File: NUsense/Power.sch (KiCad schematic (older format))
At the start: 36 parts, among them Q1201 BC807, Q1202 2N3055, Q1203 Q_NMOS_GDS, Q1204 Q_NMOS_GDS, Q1205 2N2219, Q1206 Q_PMOS_GDS, SW1201 SW_SPDT, U1201 LD1086D2M33

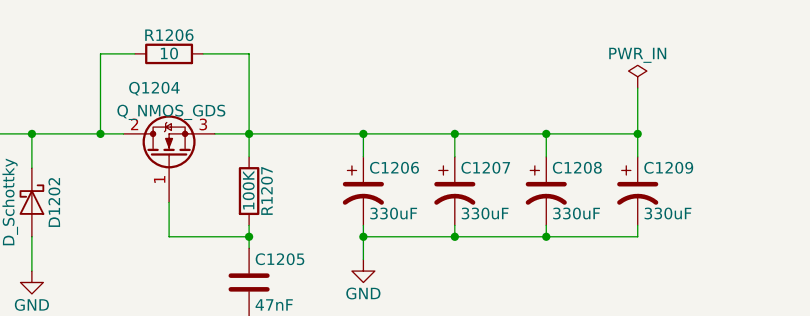
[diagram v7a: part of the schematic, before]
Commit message: Add LED and Button
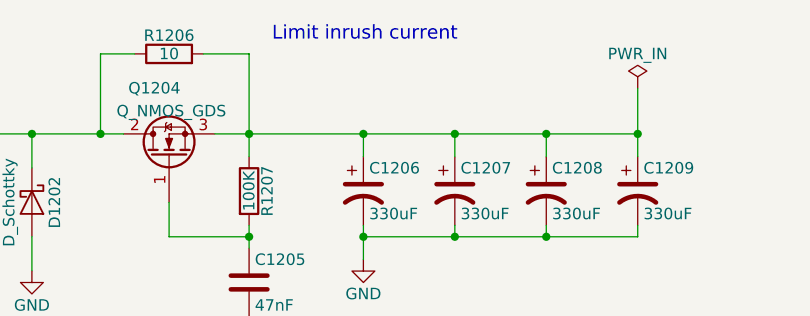
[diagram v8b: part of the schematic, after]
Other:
- note added: "Limit inrush current"
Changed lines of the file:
@@
 $EndDescr
 $Comp
-L GND #PWR0113
+L GND #PWR114
 U 1 1 5A69B4F4
 P 2700 1650
-F 0 "#PWR0113" H 2700 1400 50  0001 C CNN
+F 0 "#PWR114" H 2700 1400 50  0001 C CNN
 F 1 "GND" H 2700 1500 50  0000 C CNN
 F 2 "" H 2700 1650 50  0001 C CNN
@@
 $EndComp
 $Comp
-L GND #PWR0114
+L GND #PWR118
 U 1 1 5A69B8B6
 P 4500 3100
-F 0 "#PWR0114" H 4500 2850 50  0001 C CNN
+F 0 "#PWR118" H 4500 2850 50  0001 C CNN
 F 1 "GND" H 4500 2950 50  0000 C CNN
 F 2 "" H 4500 3100 50  0001 C CNN
@@
 $EndComp
 $Comp
-L GND #PWR0115
+L GND #PWR119
 U 1 1 5A69B8DD
 P 5400 3100
-F 0 "#PWR0115" H 5400 2850 50  0001 C CNN
+F 0 "#PWR119" H 5400 2850 50  0001 C CNN
 F 1 "GND" H 5400 2950 50  0000 C CNN
 F 2 "" H 5400 3100 50  0001 C CNN
@@
 Connection ~ 4150 1400
 $Comp
-L GND #PWR0116
+L GND #PWR120
 U 1 1 5A69BC53
 P 6150 2000
-F 0 "#PWR0116" H 6150 1750 50  0001 C CNN
+F 0 "#PWR120" H 6150 1750 50  0001 C CNN
 F 1 "GND" H 6150 1850 50  0000 C CNN
 F 2 "" H 6150 2000 50  0001 C CNN
@@
 $EndComp
 $Comp
-L GND #PWR0117
+L GND #PWR121
 U 1 1 5A69BC80
 P 6500 2000
-F 0 "#PWR0117" H 6500 1750 50  0001 C CNN
+F 0 "#PWR121" H 6500 1750 50  0001 C CNN
 F 1 "GND" H 6500 1850 50  0000 C CNN
 F 2 "" H 6500 2000 50  0001 C CNN
@@
 $EndComp
 $Comp
-L GND #PWR0118
+L GND #PWR122
 U 1 1 5A69C51E
 P 7400 2000
-F 0 "#PWR0118" H 7400 1750 50  0001 C CNN
+F 0 "#PWR122" H 7400 1750 50  0001 C CNN
 F 1 "GND" H 7400 1850 50  0000 C CNN
 F 2 "" H 7400 2000 50  0001 C CNN
@@
 $EndComp
 $Comp
-L GND #PWR0119
+L GND #PWR116
 U 1 1 5A6D2850
 P 3750 5000
-F 0 "#PWR0119" H 3750 4750 50  0001 C CNN
+F 0 "#PWR116" H 3750 4750 50  0001 C CNN
 F 1 "GND" H 3750 4850 50  0000 C CNN
 F 2 "" H 3750 5000 50  0001 C CNN
@@
 SMPS, Battery Output
 $Comp
-L +5V #PWR0120
+L +5V #PWR113
 U 1 1 5A71CFBC
 P 1900 6250
-F 0 "#PWR0120" H 1900 6100 50  0001 C CNN
+F 0 "#PWR113" H 1900 6100 50  0001 C CNN
 F 1 "+5V" H 1900 6390 50  0000 C CNN
 F 2 "" H 1900 6250 50  0001 C CNN
@@
 $EndComp
 $Comp
-L +3.3V #PWR0121
+L +3.3V #PWR117
 U 1 1 5A71CFF7
 P 3900 6250
-F 0 "#PWR0121" H 3900 6100 50  0001 C CNN
+F 0 "#PWR117" H 3900 6100 50  0001 C CNN
 F 1 "+3.3V" H 3900 6390 50  0000 C CNN
 F 2 "" H 3900 6250 50  0001 C CNN
@@
 $EndComp
 $Comp
-L GND #PWR0122
+L GND #PWR115
 U 1 1 5A71D094
 P 2750 6850
-F 0 "#PWR0122" H 2750 6600 50  0001 C CNN
+F 0 "#PWR115" H 2750 6600 50  0001 C CNN
 F 1 "GND" H 2750 6700 50  0000 C CNN
 F 2 "" H 2750 6850 50  0001 C CNN
@@
 Connection ~ 10600 4150
 $Comp
-L GND #PWR0123
+L GND #PWR125
 U 1 1 5A710549
 P 10600 4950
-F 0 "#PWR0123" H 10600 4700 50  0001 C CNN
+F 0 "#PWR125" H 10600 4700 50  0001 C CNN
 F 1 "GND" H 10600 4800 50  0000 C CNN
 F 2 "" H 10600 4950 50  0001 C CNN
@@
 	11850 4900 11850 4350
 $Comp
-L DXL_PWR #FLG0124
+L DXL_PWR #FLG10
 U 1 1 5A752493
 P 12050 4700
-F 0 "#FLG0124" H 12050 4775 50  0001 C CNN
+F 0 "#FLG10" H 12050 4775 50  0001 C CNN
 F 1 "DXL_PWR" H 12050 4850 50  0000 C CNN
 F 2 "" H 12050 4700 50  0001 C CNN
@@
 	8350 2200 8350 2350
 $Comp
-L GND #PWR0125
+L GND #PWR123
 U 1 1 5A740B51
 P 8350 2350
-F 0 "#PWR0125" H 8350 2100 50  0001 C CNN
+F 0 "#PWR123" H 8350 2100 50  0001 C CNN
 F 1 "GND" H 8350 2200 50  0000 C CNN
 F 2 "" H 8350 2350 50  0001 C CNN
@@
 	8850 1800 8850 1950
 $Comp
-L GND #PWR0126
+L GND #PWR124
 U 1 1 5A740E03
 P 8850 1950
-F 0 "#PWR0126" H 8850 1700 50  0001 C CNN
+F 0 "#PWR124" H 8850 1700 50  0001 C CNN
 F 1 "GND" H 8850 1800 50  0000 C CNN
 F 2 "" H 8850 1950 50  0001 C CNN
@@
 	8850 1850 10050 1850
 $Comp
-L PWR_IN #FLG0127
+L PWR_IN #FLG8
 U 1 1 5A744163
 P 10050 1200
-F 0 "#FLG0127" H 10050 1275 50  0001 C CNN
+F 0 "#FLG8" H 10050 1275 50  0001 C CNN
 F 1 "PWR_IN" H 10050 1350 50  0000 C CNN
 F 2 "" H 10050 1200 50  0001 C CNN
@@
 $EndComp
 $Comp
-L PWR_IN #FLG0128
+L PWR_IN #FLG6
 U 1 1 5A744387
 P 2200 4550
-F 0 "#FLG0128" H 2200 4625 50  0001 C CNN
+F 0 "#FLG6" H 2200 4625 50  0001 C CNN
 F 1 "PWR_IN" H 2200 4700 50  0000 C CNN
 F 2 "" H 2200 4550 50  0001 C CNN
@@
 	2200 4550 2200 4750
 $Comp
-L PWR_POST_SW #FLG0129
+L PWR_POST_SW #FLG7
 U 1 1 5A74479F
 P 3750 4500
-F 0 "#FLG0129" H 3750 4575 50  0001 C CNN
+F 0 "#FLG7" H 3750 4575 50  0001 C CNN
 F 1 "PWR_POST_SW" H 3750 4650 50  0000 C CNN
 F 2 "" H 3750 4500 50  0001 C CNN
@@
 $EndComp
 $Comp
-L PWR_POST_SW #FLG0130
+L PWR_POST_SW #FLG9
 U 1 1 5A744814
 P 11850 3200
-F 0 "#FLG0130" H 11850 3275 50  0001 C CNN
+F 0 "#FLG9" H 11850 3275 50  0001 C CNN
 F 1 "PWR_POST_SW" H 11850 3350 50  0000 C CNN
 F 2 "" H 11850 3200 50  0001 C CNN
@@
 Text HLabel 5400 1700 0    60   BiDi ~ 0
 BATT_-
+Text Notes 8450 1000 0    60   ~ 0
+Limit inrush current
 $EndSCHEMATC
